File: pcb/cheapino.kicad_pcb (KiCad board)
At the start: 2 copper layers, 132.5 x 95.1 mm, 103 parts, among them J1 USB_C_Receptacle_USB2.0_16P, J2 DBG, K1 SW_Push, K10 SW_Push, K11 SW_Push, K12 SW_Push, K13 SW_Push, K14 SW_Push, K15 SW_Push, K16 SW_Push, K17 SW_Push, K18 SW_Push, K2 SW_Push, K3 SW_Push, K4 SW_Push, K5 SW_Push, K6 SW_Push, K7 SW_Push, K8 SW_Push, K9 SW_Push, SW1 BOOT, SW2 RST, U1 RP2040, U2 TPD2E2U06, U3 AP2112K-3.3, U4 TXS0101DBV, U5 W25Q128JVSIQ, U6 TVS0500DRV, U7 TPD6E05U06RVZ, Y1 12MHz

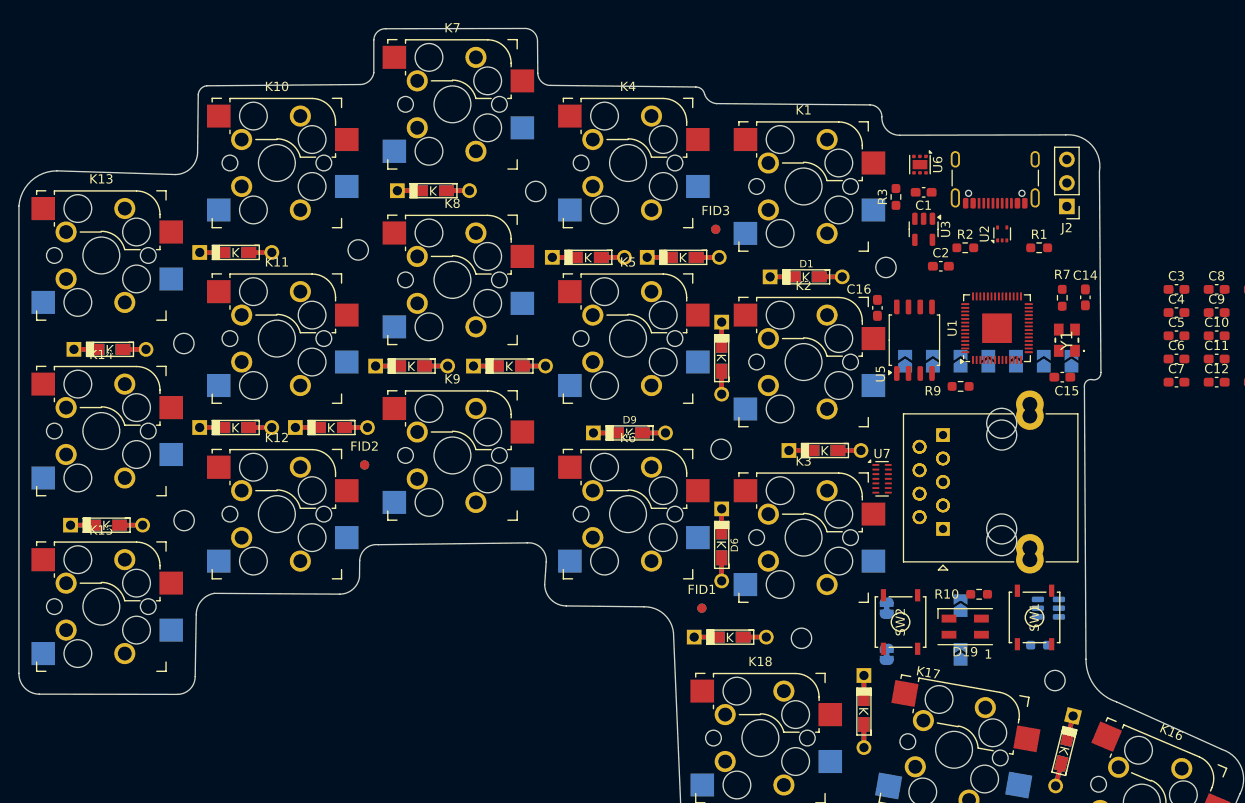
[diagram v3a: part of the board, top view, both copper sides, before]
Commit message: Replacing 6 channel ESD protection with multiple 2 channel ones.
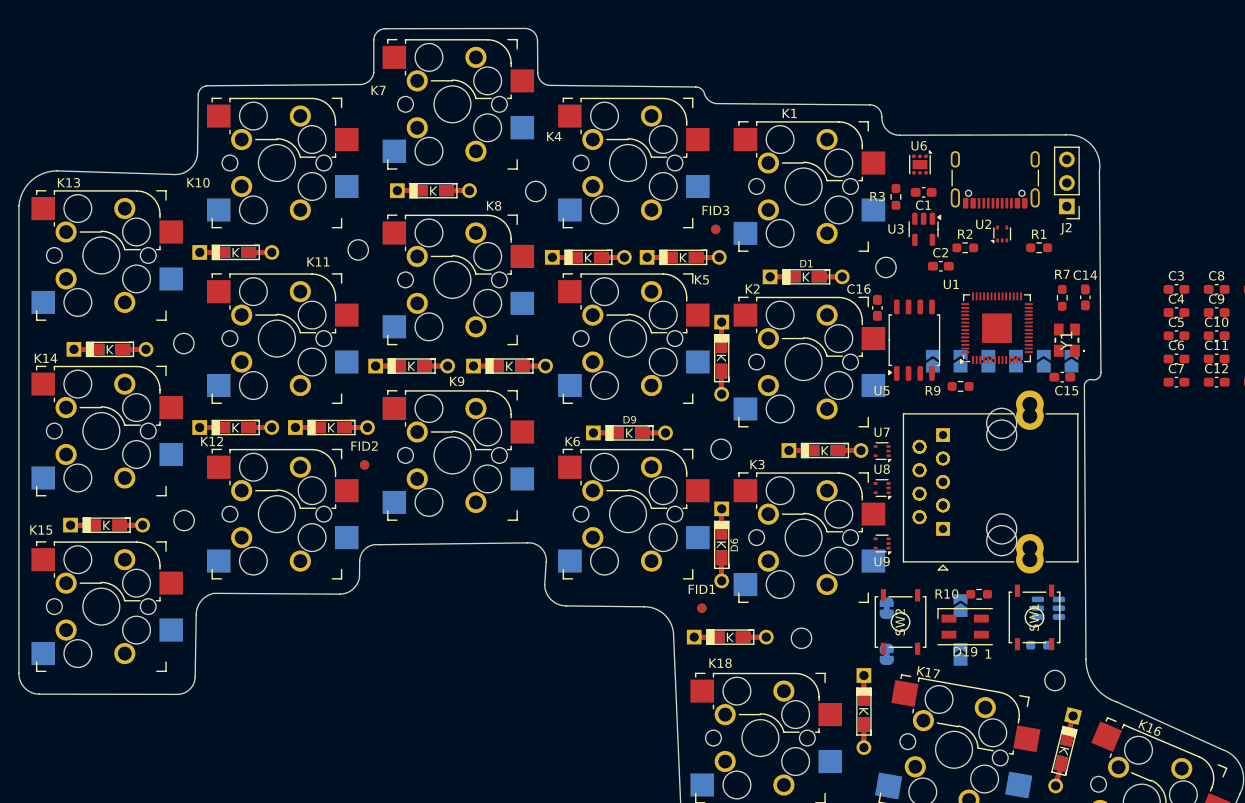
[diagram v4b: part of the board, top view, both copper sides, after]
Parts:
- removed JP7: SolderJumper_2_Open, Jumper:SolderJumper-2_P1.3mm_Open_TrianglePad1.0x1.5mm
- removed REF** (x9): MountingHole_2.2mm_M2, MountingHole:MountingHole_2.2mm_M2
- added H1: MountingHole, MountingHole:MountingHole_2.2mm_M2, F.Cu at (77.9, 79.9)
- added H2: MountingHole, MountingHole:MountingHole_2.2mm_M2, F.Cu at (78.0, 99.0)
- added H3: MountingHole, MountingHole:MountingHole_2.2mm_M2, F.Cu at (96.8, 69.7)
- added H4: MountingHole, MountingHole:MountingHole_2.2mm_M2, F.Cu at (116.0, 63.4)
- added H5: MountingHole, MountingHole:MountingHole_2.2mm_M2, F.Cu at (136.1, 91.3)
- added H6: MountingHole, MountingHole:MountingHole_2.2mm_M2, F.Cu at (144.8, 111.8)
- added H7: MountingHole, MountingHole:MountingHole_2.2mm_M2, F.Cu at (153.9, 71.6)
- added H8: MountingHole, MountingHole:MountingHole_2.2mm_M2, F.Cu at (169.2, 132.6)
- added H9: MountingHole, MountingHole:MountingHole_2.2mm_M2, F.Cu at (172.2, 116.3)
- added U8: TPD2E2U06, Package_TO_SOT_SMD:SOT-553, F.Cu at (153.5, 95.5)
- added U9: TPD2E2U06, Package_TO_SOT_SMD:SOT-553, F.Cu at (153.5, 101.5)
- U7: value TPD6E05U06RVZ -> TPD2E2U06; footprint Package_SON:Texas_R-PUSON-N14 -> Package_TO_SOT_SMD:SOT-553
- moved U7 3.00 mm to (153.5, 91.5), turned to 180 degrees
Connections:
- U7 pad 3: GND -> /ExtConnectors/C_R_ROW_3
- U7 pad 5: GND -> /ExtConnectors/C_R_ROW_2

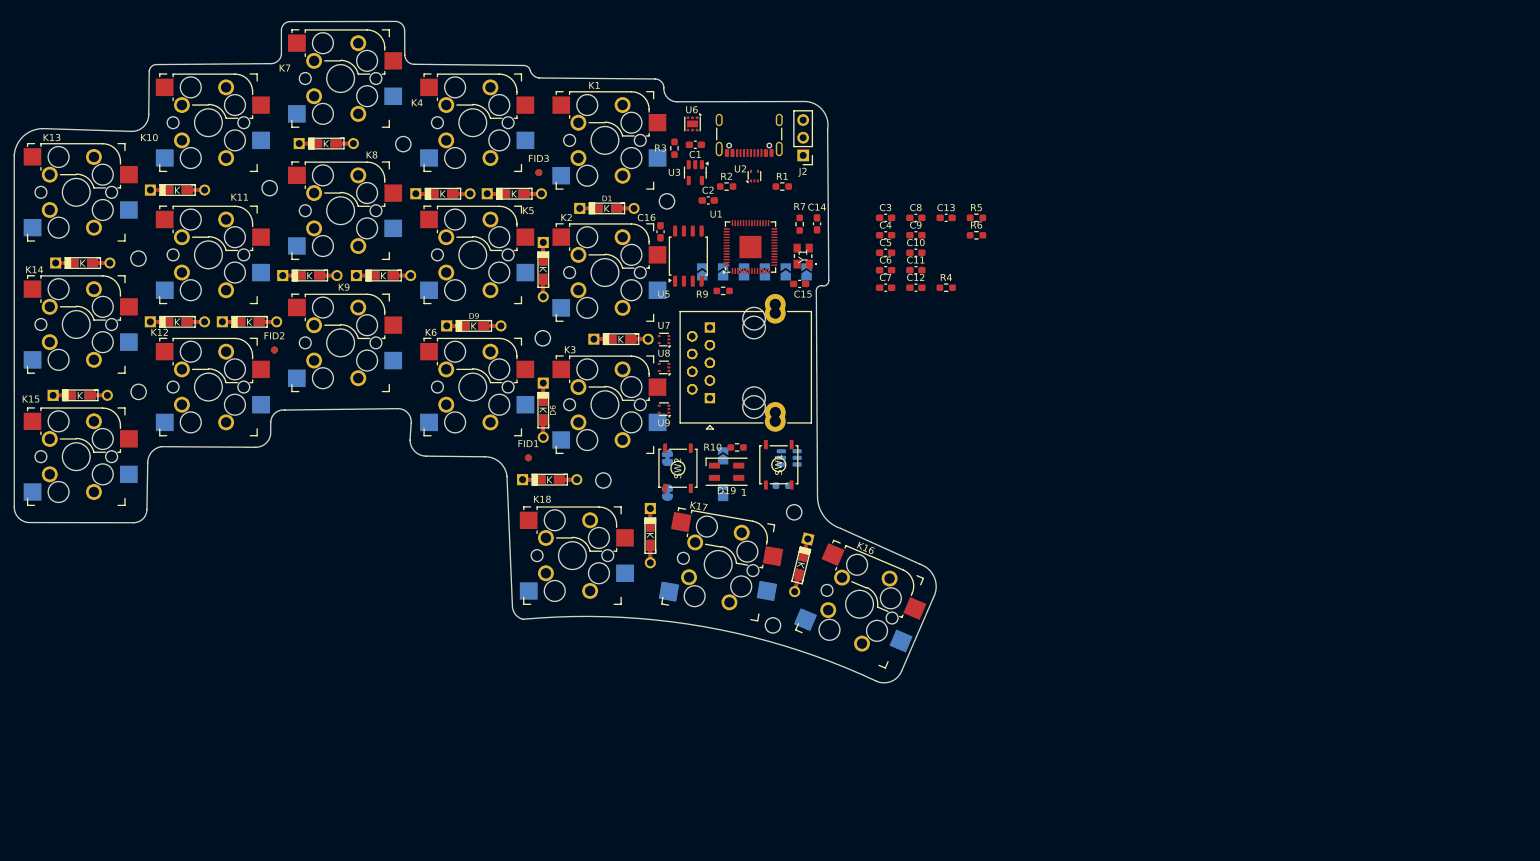
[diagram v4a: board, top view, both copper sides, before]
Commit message: Adding reversible MX Sockets and SK6812MiniE footprints, finishing the replacement of Ethernet with a TRRS connector and selectable 0Ohm resistors to swap Rx/Tx for the interconnect.
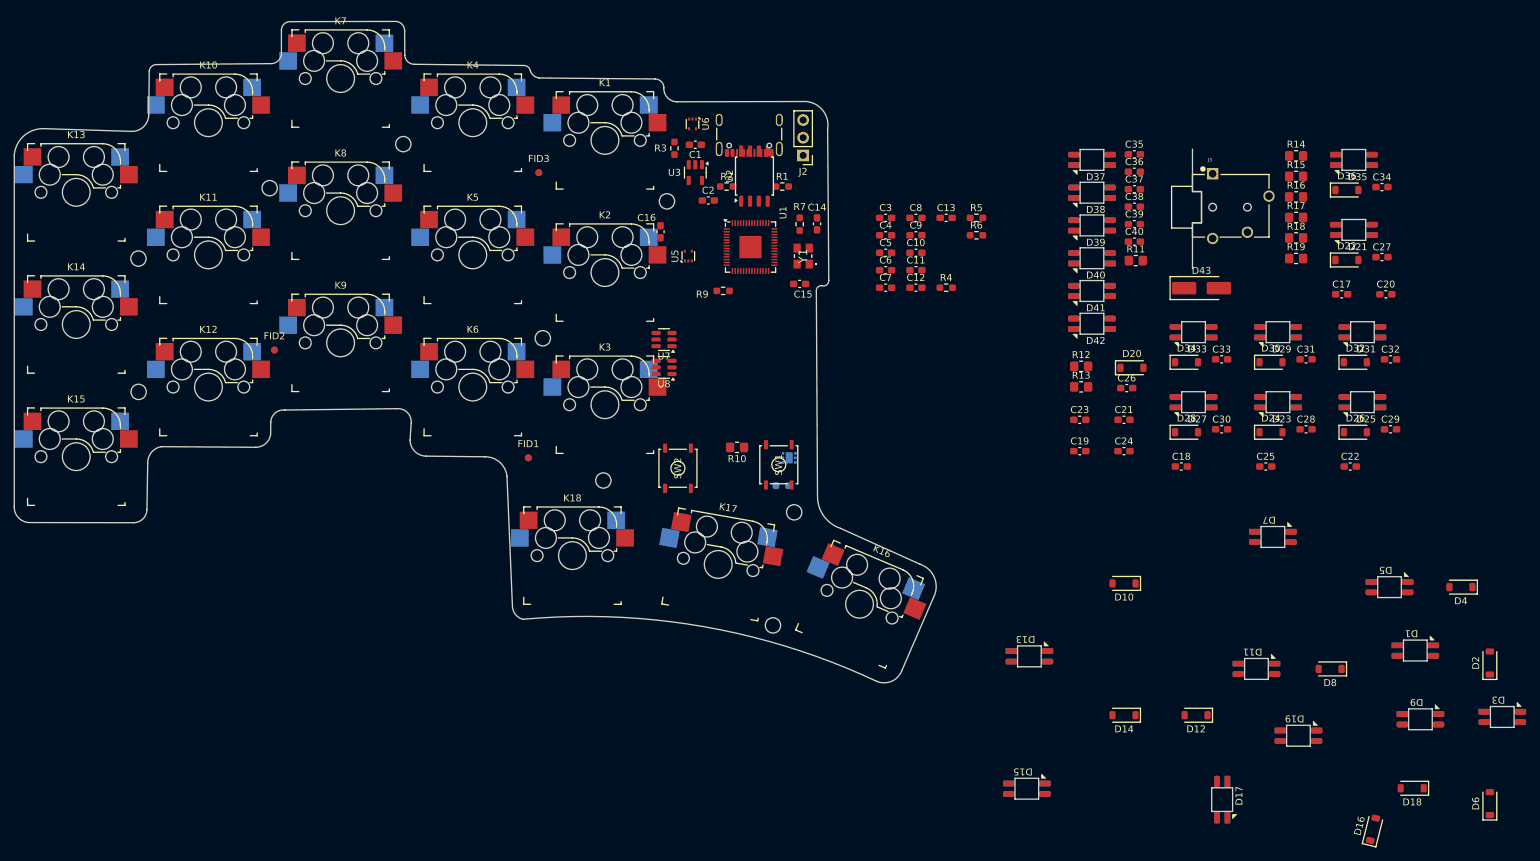
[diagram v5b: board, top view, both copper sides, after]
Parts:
- removed JP1, JP2, JP3, JP4, JP5, JP6: SolderJumper_2_Open, Jumper:SolderJumper-2_P1.3mm_Open_TrianglePad1.0x1.5mm
- removed JP10, JP8: LED_DriveAs3V3, Jumper:SolderJumper-2_P1.3mm_Bridged_RoundedPad1.0x1.5mm
- removed JP11, JP9: LED_DriveAs5V, Jumper:SolderJumper-2_P1.3mm_Open_TrianglePad1.0x1.5mm
- removed J_1_LEFT1, J_2_RIGHT1: RJ45_Shielded, Connector_RJ:RJ45_Ninigi_GE
- removed U9: TPD2E2U06, Package_TO_SOT_SMD:SOT-553
- added C17: 100nF, Capacitor_SMD:C_0603_1608Metric_Pad1.08x0.95mm_HandSolder, F.Cu at (250.9, 85.0)
- added C18: 100nF, Capacitor_SMD:C_0603_1608Metric_Pad1.08x0.95mm_HandSolder, F.Cu at (227.9, 109.8)
- added C19: 100nF, Capacitor_SMD:C_0603_1608Metric_Pad1.08x0.95mm_HandSolder, F.Cu at (213.3, 107.5)
- added C20: 100nF, Capacitor_SMD:C_0603_1608Metric_Pad1.08x0.95mm_HandSolder, F.Cu at (257.3, 85.0)
- added C21: 100nF, Capacitor_SMD:C_0603_1608Metric_Pad1.08x0.95mm_HandSolder, F.Cu at (219.6, 103.0)
- added C22: 100nF, Capacitor_SMD:C_0603_1608Metric_Pad1.08x0.95mm_HandSolder, F.Cu at (252.1, 109.8)
- added C23: 100nF, Capacitor_SMD:C_0603_1608Metric_Pad1.08x0.95mm_HandSolder, F.Cu at (213.3, 103.0)
- added C24: 100nF, Capacitor_SMD:C_0603_1608Metric_Pad1.08x0.95mm_HandSolder, F.Cu at (219.6, 107.5)
- added C25: 100nF, Capacitor_SMD:C_0603_1608Metric_Pad1.08x0.95mm_HandSolder, F.Cu at (240.0, 109.8)
- added C26: 100nF, Capacitor_SMD:C_0603_1608Metric_Pad1.08x0.95mm_HandSolder, F.Cu at (220.0, 98.5)
- added C27: 100nF, Capacitor_SMD:C_0603_1608Metric_Pad1.08x0.95mm_HandSolder, F.Cu at (256.7, 79.6)
- added C28: 100nF, Capacitor_SMD:C_0603_1608Metric_Pad1.08x0.95mm_HandSolder, F.Cu at (245.8, 104.4)
- added C29: 100nF, Capacitor_SMD:C_0603_1608Metric_Pad1.08x0.95mm_HandSolder, F.Cu at (257.9, 104.4)
- added C30: 100nF, Capacitor_SMD:C_0603_1608Metric_Pad1.08x0.95mm_HandSolder, F.Cu at (233.7, 104.4)
- added C31: 100nF, Capacitor_SMD:C_0603_1608Metric_Pad1.08x0.95mm_HandSolder, F.Cu at (245.8, 94.3)
- added C32: 100nF, Capacitor_SMD:C_0603_1608Metric_Pad1.08x0.95mm_HandSolder, F.Cu at (257.9, 94.3)
- added C33: 100nF, Capacitor_SMD:C_0603_1608Metric_Pad1.08x0.95mm_HandSolder, F.Cu at (233.7, 94.3)
- added C34: 100nF, Capacitor_SMD:C_0603_1608Metric_Pad1.08x0.95mm_HandSolder, F.Cu at (256.7, 69.6)
- added C35: 100nF, Capacitor_SMD:C_0603_1608Metric_Pad1.08x0.95mm_HandSolder, F.Cu at (221.1, 64.9)
- added C36: 100nF, Capacitor_SMD:C_0603_1608Metric_Pad1.08x0.95mm_HandSolder, F.Cu at (221.1, 67.4)
- added C37: 100nF, Capacitor_SMD:C_0603_1608Metric_Pad1.08x0.95mm_HandSolder, F.Cu at (221.1, 69.9)
- added C38: 100nF, Capacitor_SMD:C_0603_1608Metric_Pad1.08x0.95mm_HandSolder, F.Cu at (221.1, 72.4)
- added C39: 100nF, Capacitor_SMD:C_0603_1608Metric_Pad1.08x0.95mm_HandSolder, F.Cu at (221.1, 74.9)
- added C40: 100nF, Capacitor_SMD:C_0603_1608Metric_Pad1.08x0.95mm_HandSolder, F.Cu at (221.1, 77.4)
- added D20: 1N4148W, Diode_SMD:D_SOD-123, F.Cu at (220.8, 95.5)
- added D21: ~, Extra:SK6812-MINI-E_ReverseMount_reversible, F.Cu at (252.7, 75.7)
- added D22: 1N4148W, Diode_SMD:D_SOD-123, F.Cu at (251.7, 80.1)
- added D23: ~, Extra:SK6812-MINI-E_ReverseMount_reversible, F.Cu at (241.8, 100.5)
- added D24: 1N4148W, Diode_SMD:D_SOD-123, F.Cu at (240.8, 104.8)
- added D25: ~, Extra:SK6812-MINI-E_ReverseMount_reversible, F.Cu at (253.9, 100.5)
- added D26: 1N4148W, Diode_SMD:D_SOD-123, F.Cu at (252.9, 104.8)
- added D27: ~, Extra:SK6812-MINI-E_ReverseMount_reversible, F.Cu at (229.6, 100.5)
- added D28: 1N4148W, Diode_SMD:D_SOD-123, F.Cu at (228.6, 104.8)
- added D29: ~, Extra:SK6812-MINI-E_ReverseMount_reversible, F.Cu at (241.8, 90.4)
- added D30: 1N4148W, Diode_SMD:D_SOD-123, F.Cu at (240.8, 94.8)
- added D31: ~, Extra:SK6812-MINI-E_ReverseMount_reversible, F.Cu at (253.9, 90.4)
- added D32: 1N4148W, Diode_SMD:D_SOD-123, F.Cu at (252.9, 94.8)
- added D33: ~, Extra:SK6812-MINI-E_ReverseMount_reversible, F.Cu at (229.6, 90.4)
- added D34: 1N4148W, Diode_SMD:D_SOD-123, F.Cu at (228.6, 94.8)
- added D35: ~, Extra:SK6812-MINI-E_ReverseMount_reversible, F.Cu at (252.7, 65.7)
- added D36: 1N4148W, Diode_SMD:D_SOD-123, F.Cu at (251.7, 70.0)
- added D37: ~, Extra:SK6812-MINI-E_ReverseMount_reversible, F.Cu at (215.0, 65.7)
- added D38: ~, Extra:SK6812-MINI-E_ReverseMount_reversible, F.Cu at (215.0, 70.4)
- added D39: ~, Extra:SK6812-MINI-E_ReverseMount_reversible, F.Cu at (215.0, 75.1)
- added D40: ~, Extra:SK6812-MINI-E_ReverseMount_reversible, F.Cu at (215.0, 79.8)
- added D41: ~, Extra:SK6812-MINI-E_ReverseMount_reversible, F.Cu at (215.0, 84.5)
- added D42: ~, Extra:SK6812-MINI-E_ReverseMount_reversible, F.Cu at (215.0, 89.2)
- added D43: SK34A-LTP, Diode_SMD:D_SMA_Handsoldering, F.Cu at (230.8, 84.1)
- added J3: SJ-43514, Extra:CUI_SJ-43514, F.Cu at (235.0, 72.5)
- added R11: 470, Resistor_SMD:R_0805_2012Metric_Pad1.20x1.40mm_HandSolder, F.Cu at (221.3, 80.2)
- added R12: 470, Resistor_SMD:R_0805_2012Metric_Pad1.20x1.40mm_HandSolder, F.Cu at (213.5, 95.3)
- added R13: 470, Resistor_SMD:R_0805_2012Metric_Pad1.20x1.40mm_HandSolder, F.Cu at (213.5, 98.3)
- added R14: 5k6, Resistor_SMD:R_0805_2012Metric_Pad1.20x1.40mm_HandSolder, F.Cu at (244.4, 65.1)
- added R15: 10k, Resistor_SMD:R_0805_2012Metric_Pad1.20x1.40mm_HandSolder, F.Cu at (244.4, 68.0)
- added R16: 0, Resistor_SMD:R_0805_2012Metric_Pad1.20x1.40mm_HandSolder, F.Cu at (244.4, 71.0)
- added R17: 0, Resistor_SMD:R_0805_2012Metric_Pad1.20x1.40mm_HandSolder, F.Cu at (244.4, 73.9)
- added R18: 0, Resistor_SMD:R_0805_2012Metric_Pad1.20x1.40mm_HandSolder, F.Cu at (244.4, 76.9)
- added R19: 0, Resistor_SMD:R_0805_2012Metric_Pad1.20x1.40mm_HandSolder, F.Cu at (244.4, 79.8)
- D1, D11, D13, D15, D17, D3, D5, D7, D9: value DIODE -> ~; footprint keebio:Diode-dual -> Extra:SK6812-MINI-E_ReverseMount_reversible
- D10, D12, D14, D16, D18, D2, D4, D6, D8: value DIODE -> 1N4148W; footprint keebio:Diode-dual -> Diode_SMD:D_SOD-123
- D19: value SK6812MINI -> ~; footprint LED_SMD:LED_SK6812MINI_PLCC4_3.5x3.5mm_P1.75mm -> Extra:SK6812-MINI-E_ReverseMount_reversible
- K1, K10, K11, K12, K13, K14, K15, K16, K17, K18, K2, K3, K4, K5, K6, K7, K8, K9: footprint keyswitches:Kailh_socket_MX_optional_reversible -> Extra:Kailh_socket_MX_reversible
- R10: value 1k -> 470; footprint Resistor_SMD:R_0603_1608Metric_Pad0.98x0.95mm_HandSolder -> Resistor_SMD:R_0805_2012Metric_Pad1.20x1.40mm_HandSolder
- R8: value 470 -> 10k
- R9: value 10k -> 1k
- U2: value TPD2E2U06 -> W25Q128JVSIQ; footprint Package_TO_SOT_SMD:SOT-553 -> Package_SO:SOIC-8_5.23x5.23mm_P1.27mm
- U4: value TXS0101DBV -> TVS0500DRV; footprint Package_TO_SOT_SMD:SOT-23-6 -> Package_SON:WSON-6-1EP_2x2mm_P0.65mm_EP1x1.6mm
- U5: value W25Q128JVSIQ -> TPD2E2U06; footprint Package_SO:SOIC-8_5.23x5.23mm_P1.27mm -> Package_TO_SOT_SMD:SOT-553
- U6: value TVS0500DRV -> TPD2E2U06; footprint Package_SON:WSON-6-1EP_2x2mm_P0.65mm_EP1x1.6mm -> Package_TO_SOT_SMD:SOT-553
- U7, U8: value TPD2E2U06 -> TXS0101DBV; footprint Package_TO_SOT_SMD:SOT-553 -> Package_TO_SOT_SMD:SOT-23-6
- moved D11 147.4 mm to (238.7, 138.8)
- moved D13 147.4 mm to (206.0, 137.0)
- moved D14 147.4 mm to (219.6, 145.5)
- moved D15 147.4 mm to (205.7, 156.1)
- moved D2 147.4 mm to (272.2, 138.0)
- moved D4 147.4 mm to (268.1, 127.1)
- moved D6 147.4 mm to (272.2, 158.2)
- moved D7 147.4 mm to (241.0, 119.9)
- moved D8 147.4 mm to (249.3, 138.8)
- moved D9 147.4 mm to (262.2, 146.1)
- moved D10 147.4 mm to (219.6, 126.6)
- moved D12 147.4 mm to (230.0, 145.5)
- moved D5 147.4 mm to (257.8, 127.1)
- moved D3 137.8 mm to (274.0, 145.8)
- moved D1 132.5 mm to (261.5, 136.2)
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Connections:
- net Net-(J2-Pin_1) renamed /ExtConnectors/SWCLK
- net Net-(J2-Pin_3) renamed /ExtConnectors/SWD
- C1 pad 1: VBUS -> VSYS
- D1 pad 1: /KeySwitches/ROW_1 -> GND
- D1 pad 2: Net-(D1-A) -> /KeySwitches/KeySwitch_RGB_4_1/LED_Out
- D11 pad 1: Net-(D11-K) -> GND
- D11 pad 2: /KeySwitches/ROW_2 -> /KeySwitches/KeySwitch_RGB_1_1/LED_In
- D12 pad 2: /KeySwitches/ROW_3 -> /KeySwitches/ROW_1
- D13 pad 1: /KeySwitches/ROW_1 -> GND
- D13 pad 2: Net-(D13-A) -> /KeySwitches/KeySwitch_RGB_1_2/LED_In
- D14 pad 1: /KeySwitches/ROW_2 -> Net-(D14-K)
- D14 pad 2: Net-(D14-A) -> /KeySwitches/ROW_2
- D15 pad 1: /KeySwitches/ROW_3 -> GND
- D15 pad 2: Net-(D15-A) -> /KeySwitches/KeySwitch_RGB_2_2/LED_In
- D16 pad 2: /KeySwitches/ROW_1 -> /KeySwitches/ROW_2
- D17 pad 1: Net-(D17-K) -> GND
- D17 pad 2: /KeySwitches/ROW_2 -> /KeySwitches/KeySwitch_RGB_4_2/LED_In
- D18 pad 2: /KeySwitches/ROW_3 -> /KeySwitches/ROW_2
- D19 pad 1: unconnected-(D19-DOUT-Pad1) -> GND
- D19 pad 2: GND -> /KeySwitches/KeySwitch_RGB_3_2/LED_In
- D19 pad 3: Net-(D19-DIN) -> VSYS
- D19 pad 4: Net-(D19-VDD) -> /KeySwitches/KeySwitch_RGB_2_2/LED_In
- D2 pad 1: /KeySwitches/ROW_2 -> Net-(D2-K)
- D2 pad 2: Net-(D2-A) -> /KeySwitches/ROW_1
- D3 pad 1: /KeySwitches/ROW_3 -> GND
- D3 pad 2: Net-(D3-A) -> /KeySwitches/KeySwitch_RGB_5_1/LED_Out
- D5 pad 1: Net-(D5-K) -> GND
- D5 pad 2: /KeySwitches/ROW_2 -> /KeySwitches/KeySwitch_RGB_3_1/LED_Out
- D6 pad 2: /KeySwitches/ROW_3 -> /KeySwitches/ROW_1
- D7 pad 1: /KeySwitches/ROW_1 -> GND
- D7 pad 2: Net-(D7-A) -> /KeySwitches/KeySwitch_RGB_2_1/LED_Out
- D8 pad 1: /KeySwitches/ROW_2 -> Net-(D8-K)
- D8 pad 2: Net-(D8-A) -> /KeySwitches/ROW_1
- D9 pad 1: /KeySwitches/ROW_3 -> GND
- D9 pad 2: Net-(D9-A) -> /KeySwitches/KeySwitch_RGB_1_1/LED_Out
- J1 pad S1: GND -> unconnected-(J1-SHIELD-PadS1)_3
- K1 pad 1: /KeySwitches/COL_3 -> /KeySwitches/COL_5
- K1 pad 2: Net-(D1-A) -> Net-(D2-K)
- K10 pad 1: /KeySwitches/COL_2 -> /KeySwitches/COL_3
- K10 pad 2: Net-(D10-K) -> Net-(D20-K)
- K11 pad 1: /KeySwitches/COL_2 -> /KeySwitches/COL_5
- K11 pad 2: Net-(D11-K) -> Net-(D22-K)
- K12 pad 1: /KeySwitches/COL_2 -> /KeySwitches/COL_6
- K12 pad 2: Net-(D12-K) -> Net-(D24-K)
- K13 pad 2: Net-(D13-A) -> Net-(D26-K)
- K14 pad 1: /KeySwitches/COL_1 -> /KeySwitches/COL_2
- K14 pad 2: Net-(D14-A) -> Net-(D28-K)
- K15 pad 1: /KeySwitches/COL_1 -> /KeySwitches/COL_4
- K15 pad 2: Net-(D15-A) -> Net-(D30-K)
- K16 pad 1: /KeySwitches/COL_1 -> /KeySwitches/COL_3
- K16 pad 2: Net-(D16-K) -> Net-(D32-K)
- K17 pad 1: /KeySwitches/COL_1 -> /KeySwitches/COL_5
- K17 pad 2: Net-(D17-K) -> Net-(D34-K)
- K18 pad 1: /KeySwitches/COL_1 -> /KeySwitches/COL_6
- K18 pad 2: Net-(D18-K) -> Net-(D36-K)
- K2 pad 1: /KeySwitches/COL_3 -> /KeySwitches/COL_6
- K2 pad 2: Net-(D2-A) -> Net-(D4-K)
- K3 pad 1: /KeySwitches/COL_3 -> /KeySwitches/COL_4
- K3 pad 2: Net-(D3-A) -> Net-(D6-K)
- K4 pad 2: Net-(D4-K) -> Net-(D8-K)
- K5 pad 1: /KeySwitches/COL_3 -> /KeySwitches/COL_2
- K5 pad 2: Net-(D5-K) -> Net-(D10-K)
- K6 pad 1: /KeySwitches/COL_3 -> /KeySwitches/COL_1
- K6 pad 2: Net-(D6-K) -> Net-(D12-K)
- K7 pad 1: /KeySwitches/COL_2 -> /KeySwitches/COL_1
- K7 pad 2: Net-(D7-A) -> Net-(D14-K)
- K8 pad 2: Net-(D8-A) -> Net-(D16-K)
- K9 pad 1: /KeySwitches/COL_2 -> /KeySwitches/COL_4
- K9 pad 2: Net-(D9-A) -> Net-(D18-K)
- R10 pad 1: Net-(R10-Pad1) -> Net-(D37-DIN)
- R10 pad 2: /Microcontroller/QSPI_SS -> Net-(U7-B)
- R3 pad 2: VBUS -> VSYS
- R8 pad 1: Net-(JP11-A) -> +3V3
- R8 pad 2: /Lighting/DIN_5V -> /Microcontroller/QSPI_SS
- R9 pad 1: +3V3 -> Net-(R9-Pad1)
- SW1 pad 4: Net-(R10-Pad1) -> Net-(R9-Pad1)
- U1 pad 11: unconnected-(U1-GPIO8-Pad11) -> /KeySwitches/COL_3
- U1 pad 12: unconnected-(U1-GPIO9-Pad12) -> /KeySwitches/COL_4
- U1 pad 13: unconnected-(U1-GPIO10-Pad13) -> /KeySwitches/COL_5
- U1 pad 14: unconnected-(U1-GPIO11-Pad14) -> /KeySwitches/COL_6
- U1 pad 16: unconnected-(U1-GPIO13-Pad16) -> /KeySwitches/ROW_1
- U1 pad 17: /KeySwitches/COL_1 -> /KeySwitches/ROW_2
- U1 pad 18: /KeySwitches/COL_2 -> /KeySwitches/ROW_3
- U1 pad 2: /ExtConnectors/C_R_COL_1 -> /ExtConnectors/UART_Tx
- U1 pad 27: /Lighting/DIN_0 -> unconnected-(U1-GPIO16-Pad27)
- U1 pad 3: /ExtConnectors/C_R_COL_2 -> /ExtConnectors/UART_Rx
- U1 pad 34: unconnected-(U1-GPIO22-Pad34) -> /Lighting/Underglow_LED_3V3
- U1 pad 36: unconnected-(U1-GPIO24-Pad36) -> /ExtConnectors/VBUS_Sense
- U1 pad 38: /KeySwitches/COL_3 -> unconnected-(U1-GPIO26_ADC0-Pad38)
- U1 pad 39: /KeySwitches/ROW_1 -> unconnected-(U1-GPIO27_ADC1-Pad39)
- U1 pad 4: /ExtConnectors/C_R_COL_3 -> unconnected-(U1-GPIO2-Pad4)
- U1 pad 40: /KeySwitches/ROW_2 -> unconnected-(U1-GPIO28_ADC2-Pad40)
- U1 pad 41: /KeySwitches/ROW_3 -> unconnected-(U1-GPIO29_ADC3-Pad41)
- U1 pad 5: /ExtConnectors/C_R_ROW_1 -> unconnected-(U1-GPIO3-Pad5)
- U1 pad 6: /ExtConnectors/C_R_ROW_2 -> /Lighting/Per-Key_LED_3V3
- U1 pad 7: /ExtConnectors/C_R_ROW_3 -> unconnected-(U1-GPIO5-Pad7)
- U1 pad 8: unconnected-(U1-GPIO6-Pad8) -> /KeySwitches/COL_1
- U1 pad 9: unconnected-(U1-GPIO7-Pad9) -> /KeySwitches/COL_2
- U2 pad 1: GND -> /Microcontroller/QSPI_SS
- U2 pad 2: GND -> /Microcontroller/QSPI_SD1
- U2 pad 3: /ExtConnectors/D- -> /Microcontroller/QSPI_SD2
- U2 pad 5: /ExtConnectors/D+ -> /Microcontroller/QSPI_SD0
- U3 pad 1: VBUS -> VSYS
- U4 pad 1: +3V3 -> GND
- U4 pad 3: /Lighting/DIN_0 -> GND
- U4 pad 4: /Lighting/DIN_5V -> VBUS
- U4 pad 5: +3V3 -> VBUS
- U5 pad 1: /Microcontroller/QSPI_SS -> GND
- U5 pad 2: /Microcontroller/QSPI_SD1 -> GND
- U5 pad 3: /Microcontroller/QSPI_SD2 -> /ExtConnectors/D-
- U5 pad 5: /Microcontroller/QSPI_SD0 -> /ExtConnectors/D+
- U6 pad 3: GND -> /ExtConnectors/UART_Rx
- U6 pad 4: VBUS -> GND
- U6 pad 5: VBUS -> /ExtConnectors/UART_Tx
- U7 pad 1: GND -> +3V3
- U7 pad 3: /ExtConnectors/C_R_ROW_3 -> /Lighting/Underglow_LED_3V3
- U7 pad 4: GND -> Net-(U7-B)
- U7 pad 5: /ExtConnectors/C_R_ROW_2 -> +3V3
- U8 pad 1: GND -> +3V3
- U8 pad 3: /ExtConnectors/C_R_ROW_1 -> /Lighting/Per-Key_LED_3V3
- U8 pad 4: GND -> /KeySwitches/PerKey_LED_In
- U8 pad 5: /ExtConnectors/C_R_COL_3 -> +3V3
